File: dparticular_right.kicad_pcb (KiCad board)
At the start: 2 copper layers, 185.7 x 157.2 mm, 51 parts, among them J1 To Left Hand, SW1:10 Key_Ins, SW1:11 Key_Prnt, SW2:10 Key_F7, SW2:11 Key_F8, SW2:12 Key_F9, SW2:13 Key_F10, SW2:14 Key_F11, SW2:15 Key_F12, SW2:16 Key_Del, SW3:10 Key_7, SW3:11 Key_8, SW3:12 Key_9, SW3:13 Key_0, SW3:14 Key_Hyph, SW3:15 Key_Eql, SW3:16 Key_Bksp, SW3:9 Key_6, SW4:10 Key_U, SW4:11 Key_I, SW4:12 Key_O, SW4:13 Key_P, SW4:14 Key_LBrk, SW4:15 Key_RBrk, SW4:16 Key_BkSl, SW4:9 Key_Y, SW5:10 Key_J, SW5:11 Key_K, SW5:12 Key_L, SW5:13 Key_Semi, SW5:14 Key_Quot, SW5:16 Key_Entr, SW5:9 Key_H, SW6:10 Key_M, SW6:11 Key_Coma, SW6:12 Key_Per, SW6:13 Key_Slsh, SW6:14 Key_RShft, SW6:9 Key_N, SW7:11 Key_RAlt, SW7:12 Key_RWin, SW7:13 Key_Menu, SW7:14 Key_RCtrl, SW7:9 Key_RSpc, U1 MCP23018

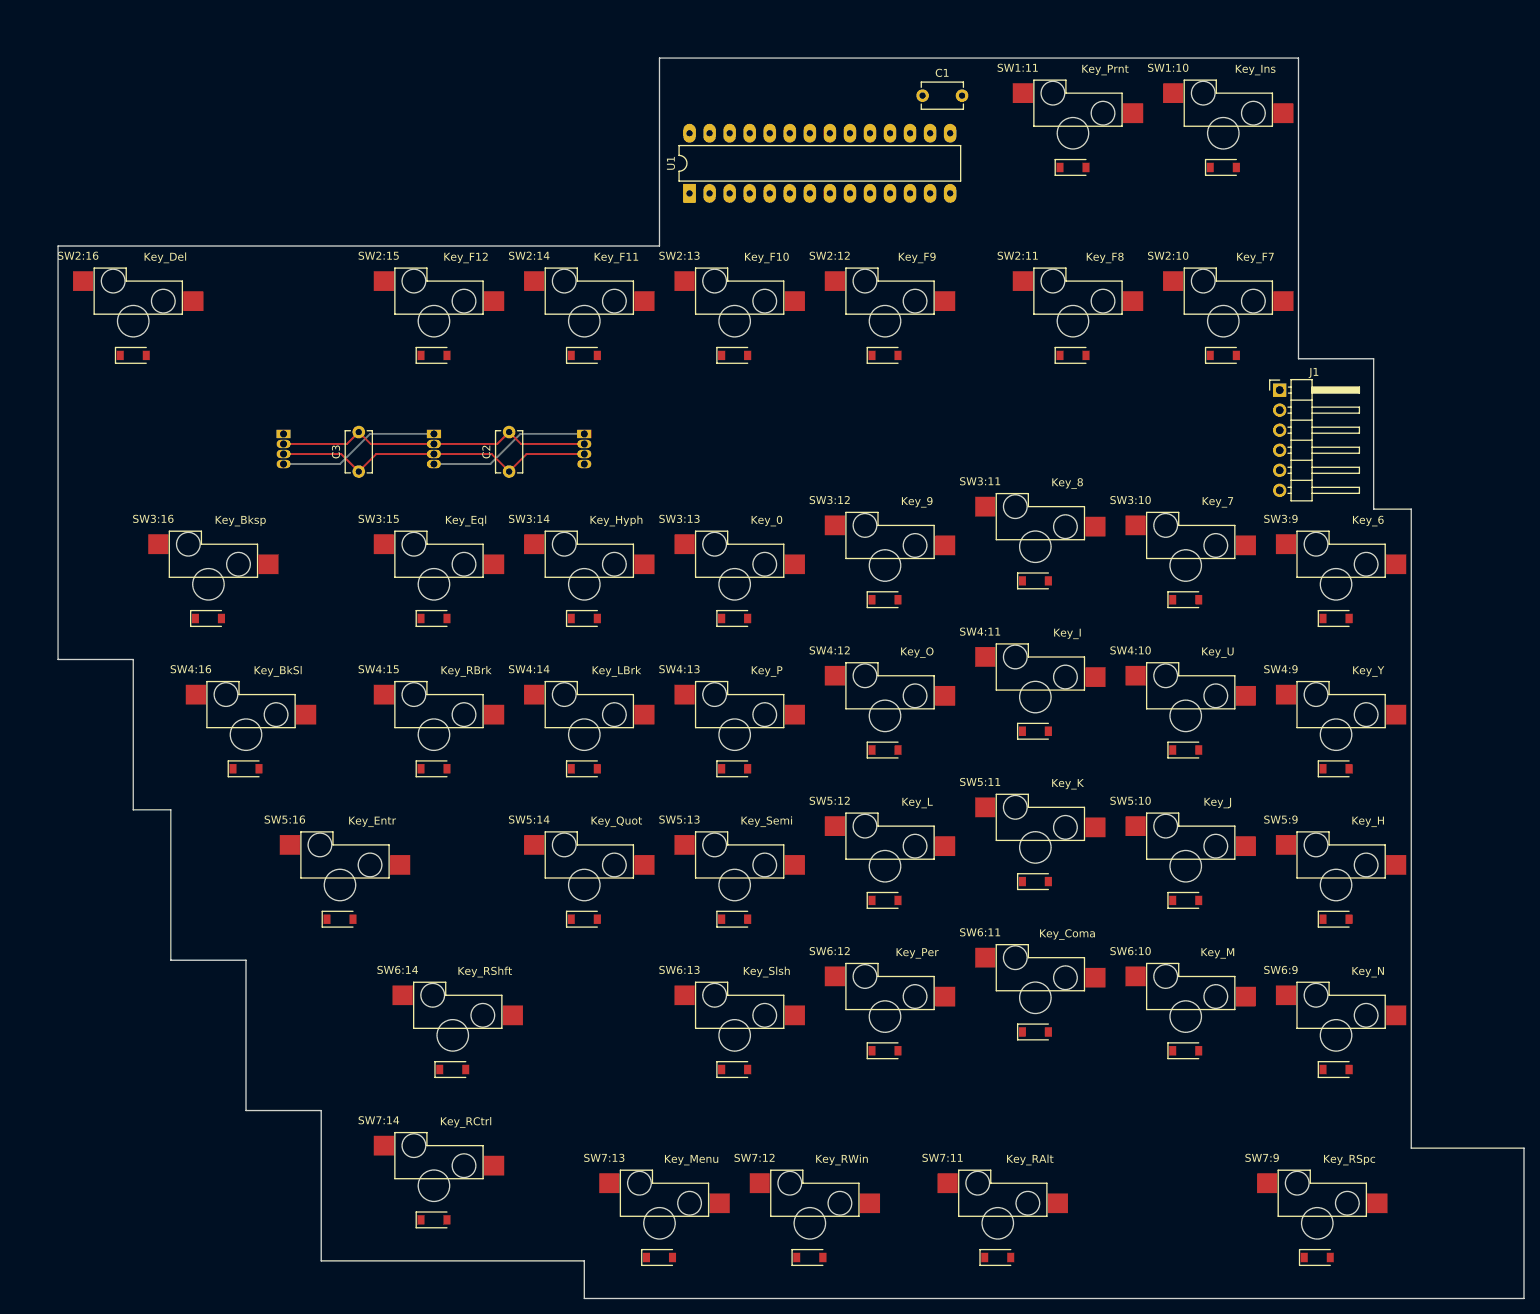
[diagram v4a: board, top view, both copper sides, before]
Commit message: right hand PCB: Column traces
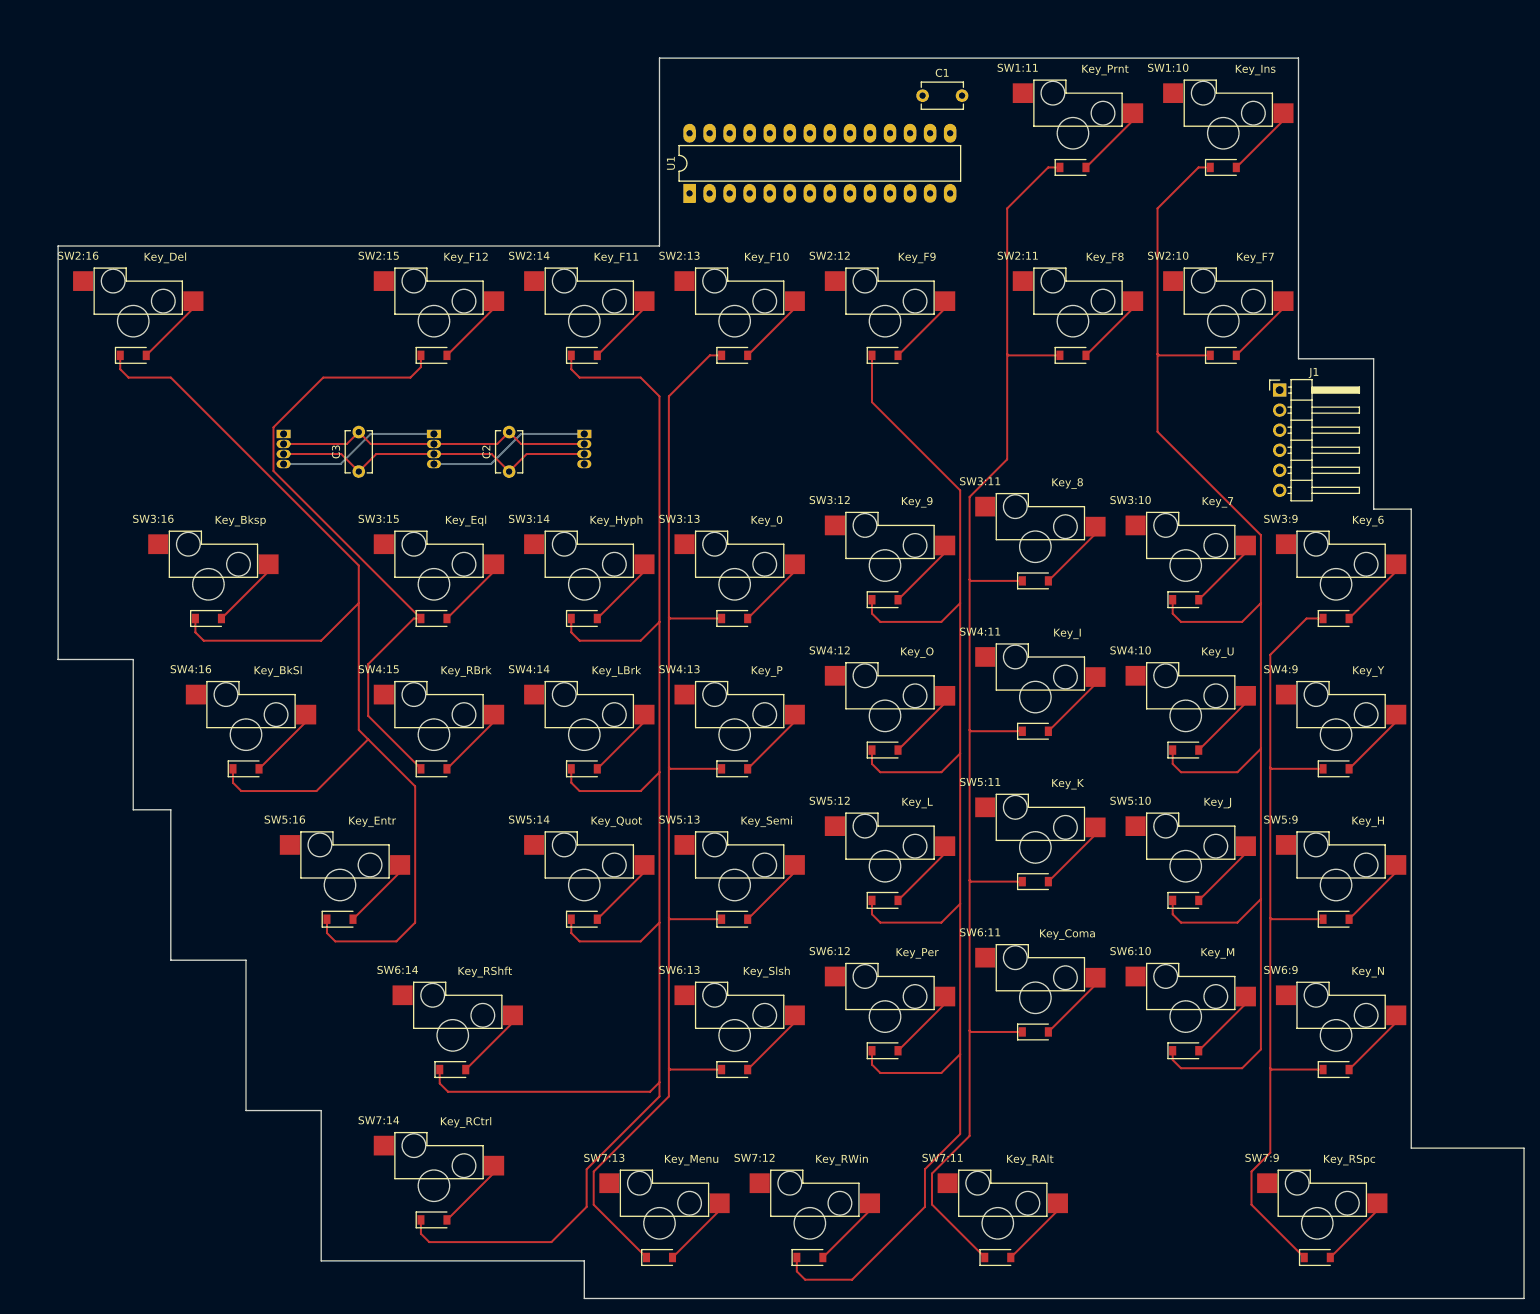
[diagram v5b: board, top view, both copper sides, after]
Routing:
- net /COL14: track 0.00 -> 219.5 mm
- net /COL12: track 0.00 -> 194.0 mm
- net /COL10: track 0.00 -> 184.9 mm
- net /COL11: track 0.00 -> 182.2 mm
- net /COL16: track 0.00 -> 151.8 mm
- net /COL13: track 0.00 -> 151.7 mm
- net /COL9: track 0.00 -> 109.0 mm
- net Net-(SW2:15-Pad4): track 0.00 -> 80.4 mm
- net Net-(SW3:16-Pad2): track 0.00 -> 9.62 mm
- net Net-(SW5:9-Pad2): track 0.00 -> 9.34 mm
- net Net-(SW5:14-Pad2): track 0.00 -> 9.34 mm
- net Net-(SW5:13-Pad2): track 0.00 -> 9.34 mm
- net Net-(SW4:12-Pad2): track 0.00 -> 9.34 mm
- net Net-(SW4:11-Pad2): track 0.00 -> 9.34 mm
- net Net-(SW4:10-Pad2): track 0.00 -> 9.34 mm
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
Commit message: Right hand completed layout
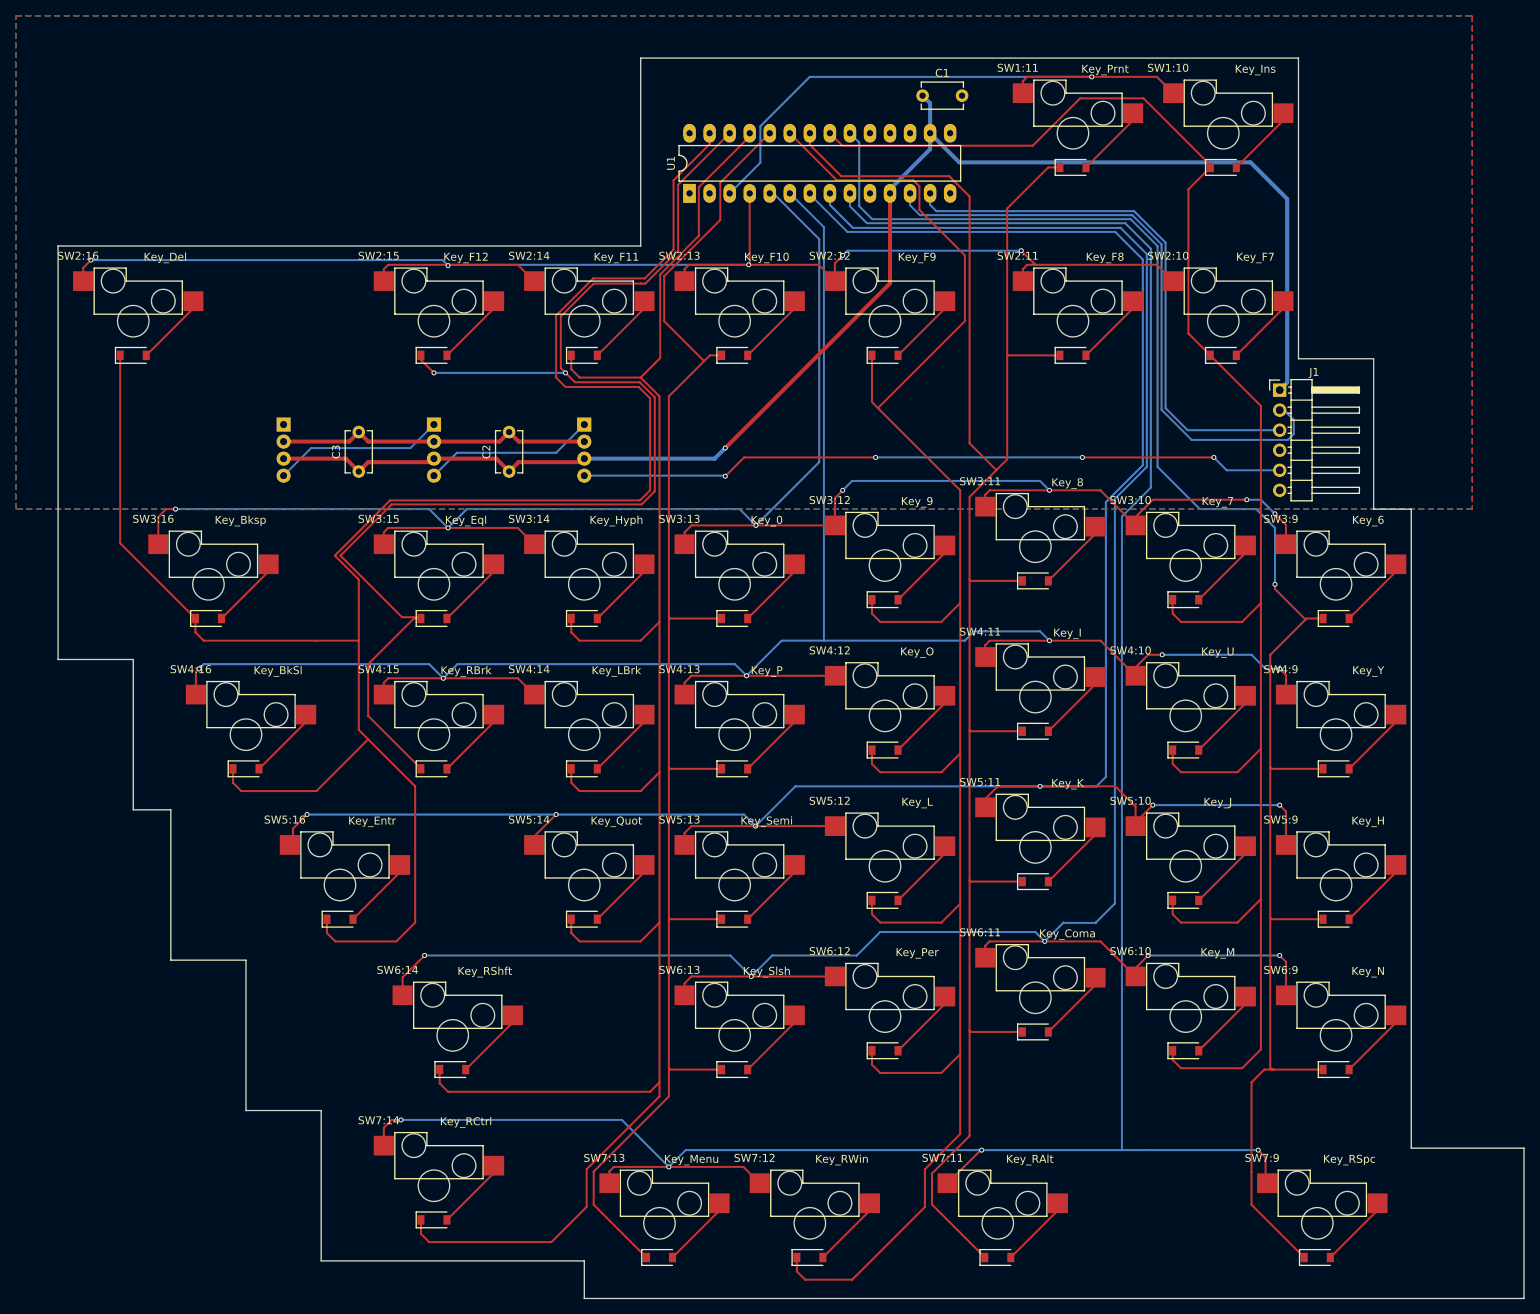
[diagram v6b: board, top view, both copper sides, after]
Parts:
- D1, D2, D3: footprint LED_THT:LED_D5.0mm-4_RGB -> LED_THT:LED_D5.0mm-4_RGB_Wide_Pins
- moved D1 1.19 mm to (95.2, 70.2)
- moved D2 1.19 mm to (76.2, 70.2)
- moved D3 1.19 mm to (57.1, 70.2)
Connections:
- SW2:15 pad 4: Net-(SW2:15-Pad4) -> /COL15
- SW3:15 pad 4: Net-(SW2:15-Pad4) -> /COL15
- SW4:15 pad 4: Net-(SW2:15-Pad4) -> /COL15
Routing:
- net /ROW7: track 0.00 -> 306.9 mm, vias 0 -> 4
- net /ROW5: track 0.00 -> 297.6 mm, vias 0 -> 6
- net /ROW6: track 0.00 -> 297.0 mm, vias 0 -> 5
- net /ROW4: track 0.00 -> 264.3 mm, vias 0 -> 6
- net /ROW3: track 0.00 -> 252.7 mm, vias 0 -> 7
- net /ROW2: track 0.00 -> 189.8 mm, vias 0 -> 5
- net /COL15: track 0.00 -> 169.2 mm, vias 0 -> 2
- net +5V: track 41.8 -> 188.3 mm, vias 0 -> 1
- net /COL9: track 109.0 -> 218.6 mm, vias 0 -> 1
- net /COL16: track 151.8 -> 258.1 mm
- net /LED_D: track 0.00 -> 89.8 mm, vias 0 -> 4
- net Net-(SW2:15-Pad4): track 80.4 -> 0.00 mm
- net /SCL: track 0.00 -> 79.1 mm
- net /ROW1: track 0.00 -> 76.3 mm, vias 0 -> 1
- net /SDA: track 0.00 -> 69.8 mm
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- added copper zone on B.Cu, net GND
- added copper zone on F.Cu, net GND
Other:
- outline, holes or cut-outs redrawn
- rule pad_to_mask_clearance: 0.05 -> 0.254

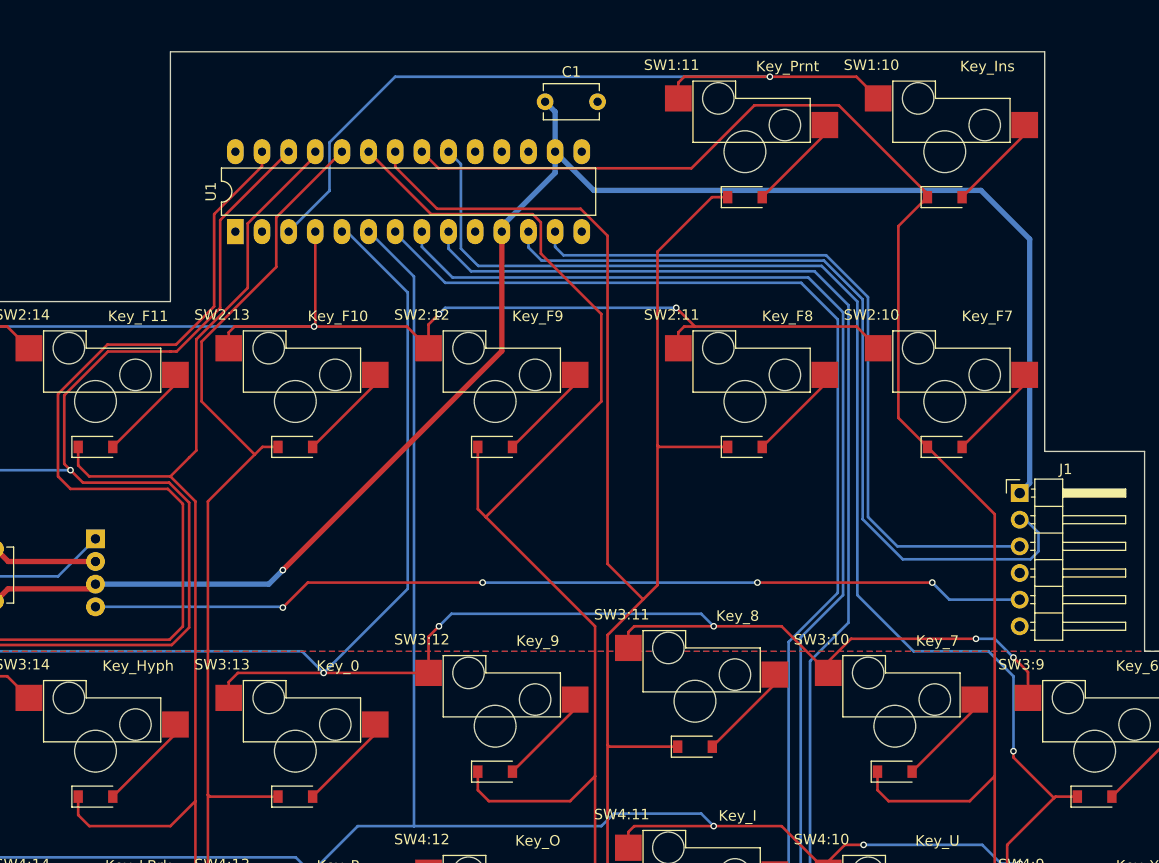
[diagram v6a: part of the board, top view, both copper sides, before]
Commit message: Right hand: don't run traces between pads
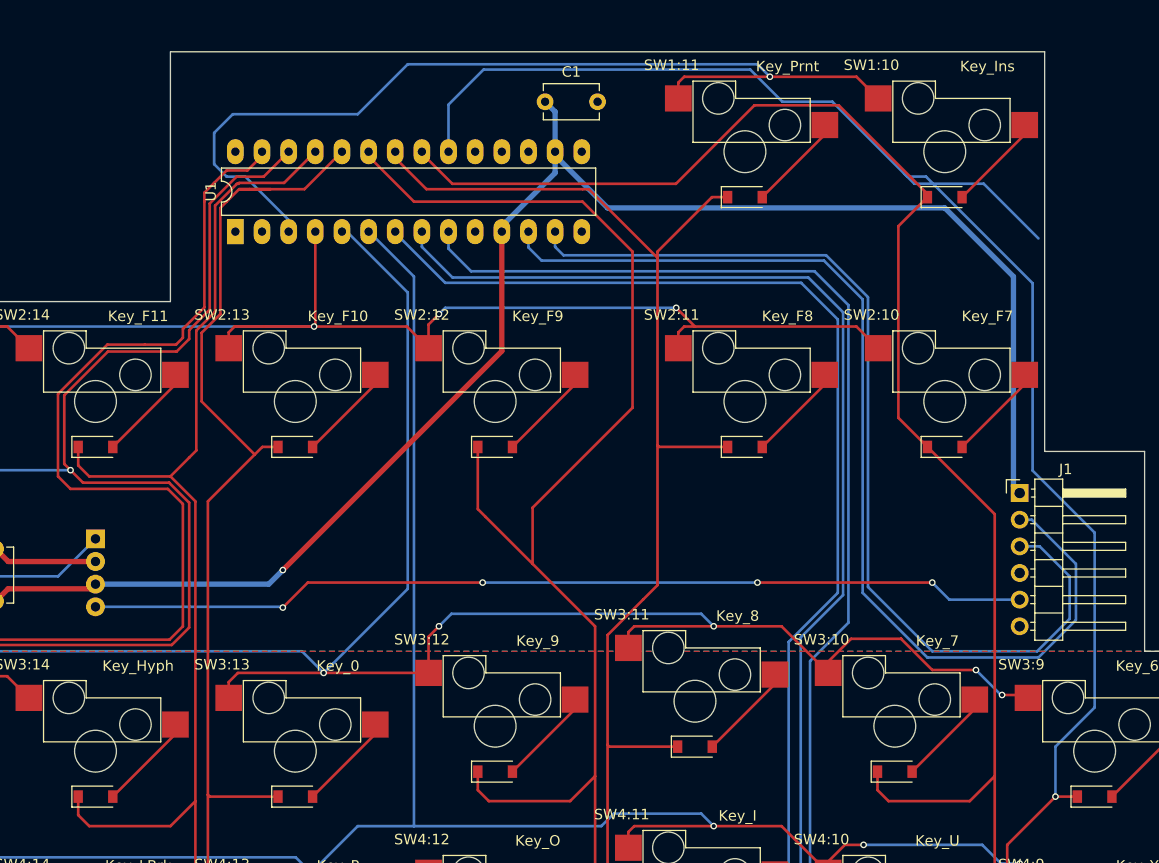
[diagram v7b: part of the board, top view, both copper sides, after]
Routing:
- net /COL11: track 242.7 -> 211.8 mm
- net /COL9: track 218.6 -> 248.9 mm
- net /SDA: track 69.8 -> 93.9 mm
- net /SCL: track 79.1 -> 100.2 mm
- net /ROW1: track 76.3 -> 91.2 mm
- net /COL12: track 248.3 -> 257.1 mm
- net /COL13: track 188.2 -> 194.8 mm
- net +5V: track 188.3 -> 184.7 mm
- net /COL14: track 256.2 -> 258.8 mm
- net /COL15: track 169.2 -> 170.7 mm
- net /ROW3: track 252.7 -> 251.3 mm
- net /COL10: track 229.2 -> 230.5 mm
- net /COL16: track 258.1 -> 259.3 mm

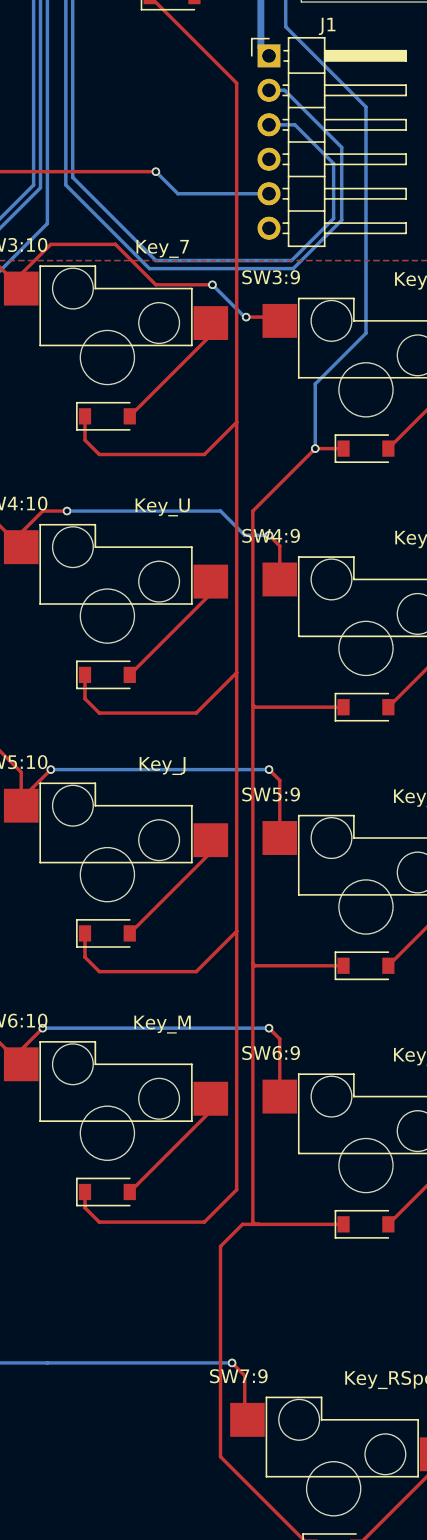
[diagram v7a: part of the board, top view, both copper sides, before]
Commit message: Right hand: eliminate right angles in columns 9 and 10
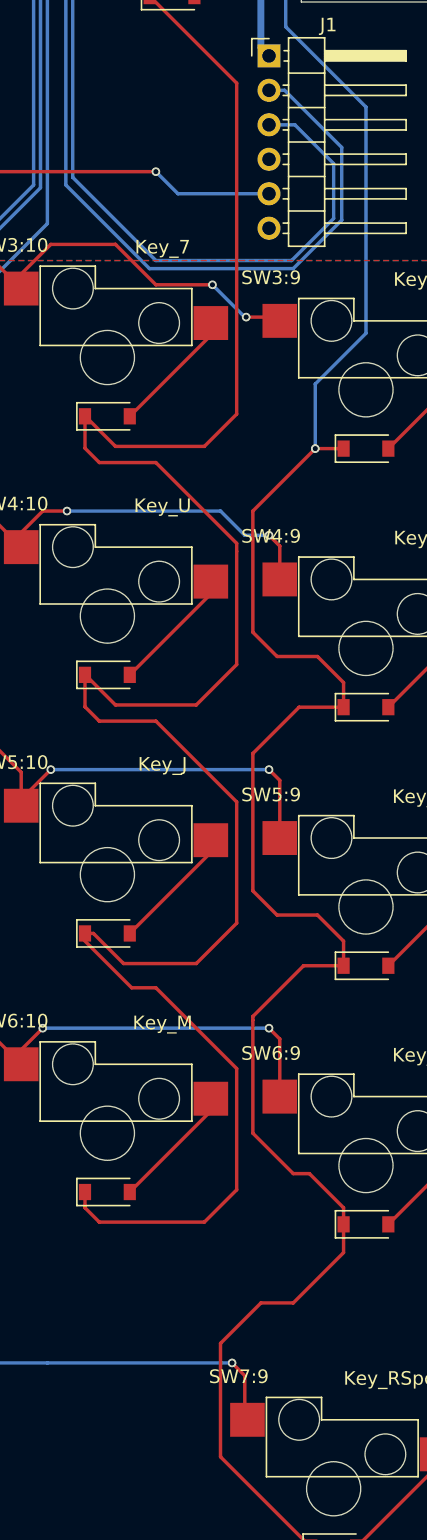
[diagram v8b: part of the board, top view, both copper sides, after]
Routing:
- net /COL10: track 230.5 -> 244.9 mm
- net /COL9: track 248.9 -> 253.7 mm
